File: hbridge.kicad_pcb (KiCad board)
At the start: 2 copper layers, 25.4 x 25.4 mm, 18 parts, among them J1 Conn_01x04_Male, J2 Screw_Terminal_01x03, Q1 2N7000, Q2 2N7000, Q3 2N3904, Q4 2N3906, Q5 2N3904, Q6 2N3906, Q7 STP20NF06, Q8 STP20NF06

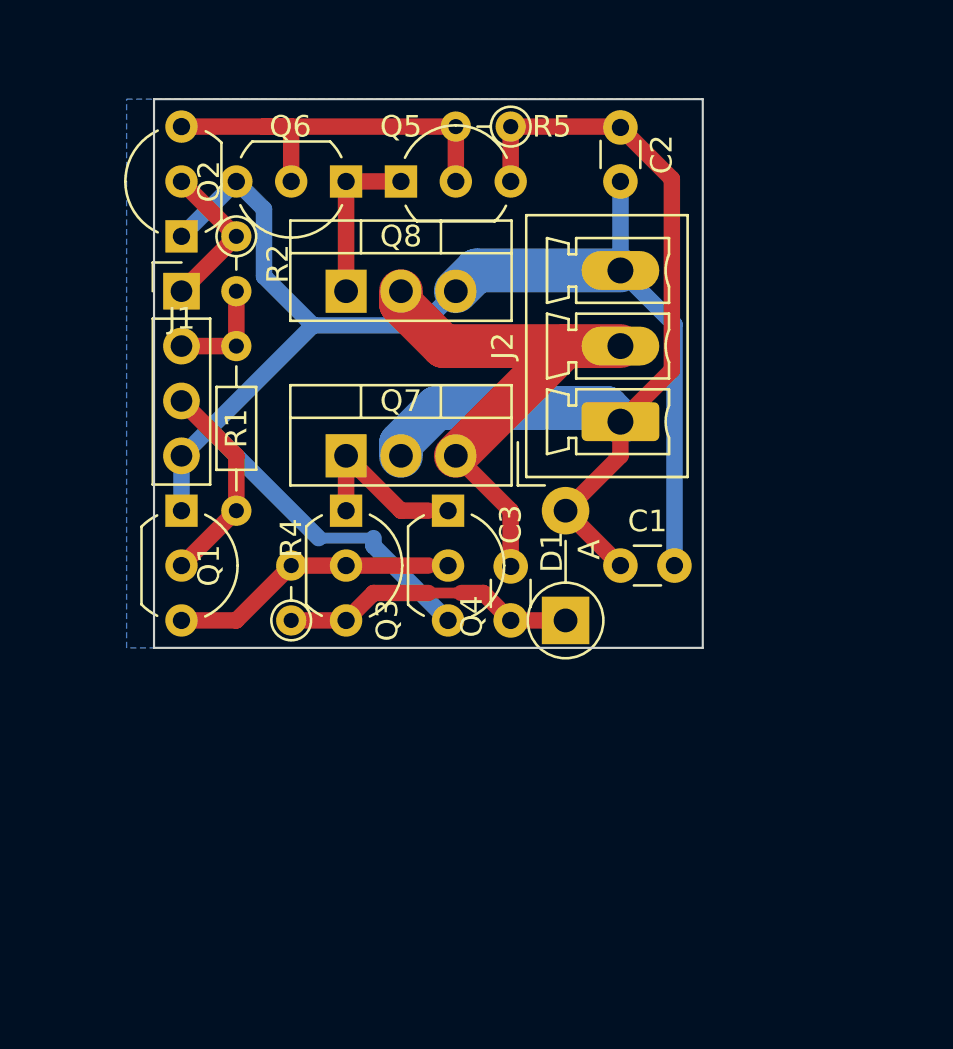
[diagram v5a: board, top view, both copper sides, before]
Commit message: Added second half-bridge to make h-bridge. Not routed yet
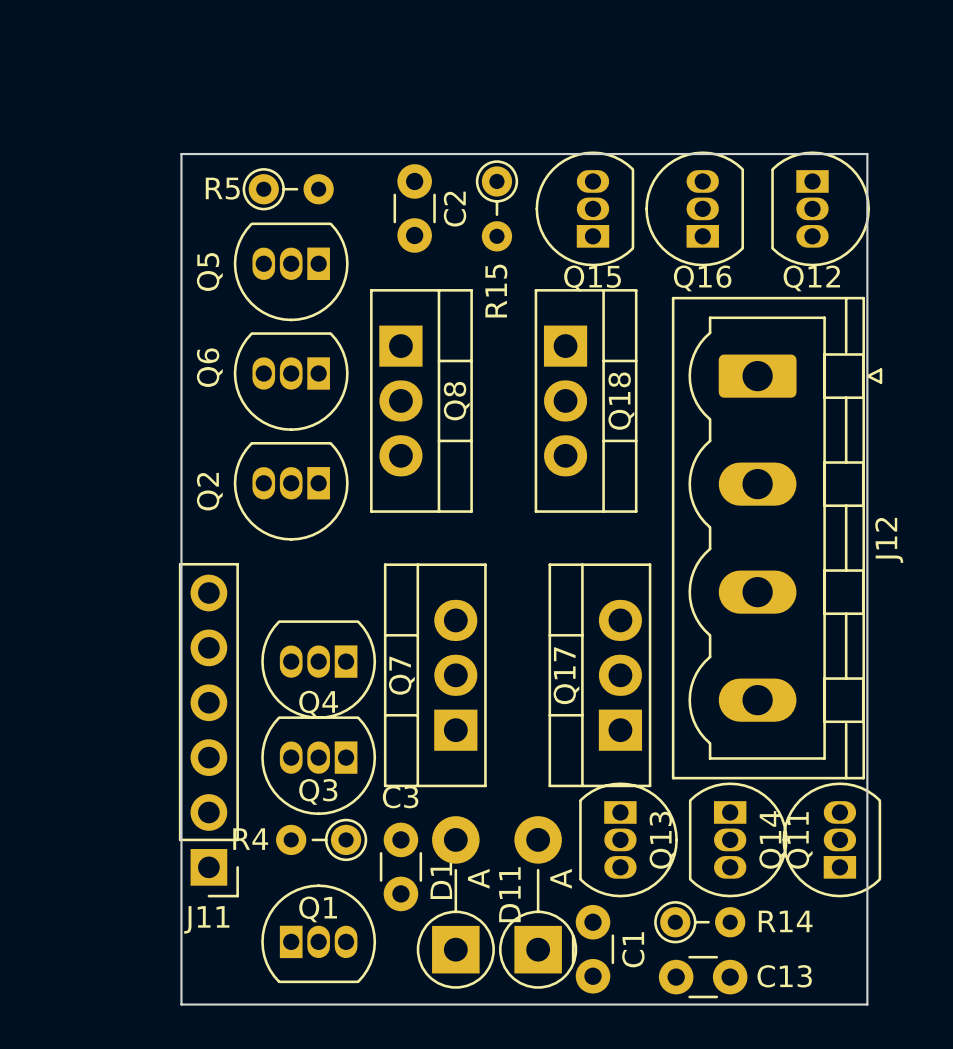
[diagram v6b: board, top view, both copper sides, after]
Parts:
- removed J1: Conn_01x04_Male, Connector_PinHeader_2.54mm:PinHeader_1x04_P2.54mm_Vertical
- removed J2: Screw_Terminal_01x03, Connector_Phoenix_MC:PhoenixContact_MCV_1,5_3-G-3.5_1x03_P3.50mm_Vertical
- removed R1: 10k, Resistor_THT:R_Axial_DIN0204_L3.6mm_D1.6mm_P7.62mm_Horizontal
- removed R2: 10k, Resistor_THT:R_Axial_DIN0204_L3.6mm_D1.6mm_P2.54mm_Vertical
- added C13: 1u, Capacitor_THT:C_Disc_D3.0mm_W1.6mm_P2.50mm, F.Cu at (124.5, 92.7)
- added D11: 1N5819, Diode_THT:D_DO-41_SOD81_P5.08mm_Vertical_AnodeUp, F.Cu at (118.1, 91.4)
- added J11: Conn_01x06_Male, Connector_PinHeader_2.54mm:PinHeader_1x06_P2.54mm_Vertical, F.Cu at (102.9, 87.6)
- added J12: Screw_Terminal_01x04, Connector_Phoenix_MSTB:PhoenixContact_MSTBVA_2,5_4-G_1x04_P5.00mm_Vertical, F.Cu at (128.3, 64.9)
- added Q11: 2N7000, Package_TO_SOT_THT:TO-92_Inline, F.Cu at (132.1, 87.6)
- added Q12: 2N7000, Package_TO_SOT_THT:TO-92_Inline, F.Cu at (130.8, 55.9)
- added Q13: 2N3904, Package_TO_SOT_THT:TO-92_Inline, F.Cu at (121.9, 85.1)
- added Q14: 2N3906, Package_TO_SOT_THT:TO-92_Inline, F.Cu at (127.0, 85.1)
- added Q15: 2N3904, Package_TO_SOT_THT:TO-92_Inline, F.Cu at (120.7, 58.4)
- added Q16: 2N3906, Package_TO_SOT_THT:TO-92_Inline, F.Cu at (125.7, 58.4)
- added Q17: STP20NF06, Package_TO_SOT_THT:TO-220-3_Vertical, F.Cu at (121.9, 81.3)
- added Q18: STP20NF06, Package_TO_SOT_THT:TO-220-3_Vertical, F.Cu at (119.4, 63.5)
- added R14: 10k, Resistor_THT:R_Axial_DIN0204_L3.6mm_D1.6mm_P2.54mm_Vertical, F.Cu at (124.5, 90.2)
- added R15: 10k, Resistor_THT:R_Axial_DIN0204_L3.6mm_D1.6mm_P2.54mm_Vertical, F.Cu at (116.2, 55.9)
- Q1, Q2, Q3, Q4, Q5, Q6: footprint Package_TO_SOT_THT:TO-92_Inline_Wide -> Package_TO_SOT_THT:TO-92_Inline
- moved Q1 20.6 mm to (106.7, 91.1), turned to 0 degrees
- moved C1 16.6 mm to (120.7, 90.2), turned to -90 degrees
- moved D1 16.1 mm to (114.3, 91.4)
- moved Q7 13.7 mm to (114.3, 81.3), turned to 90 degrees
- moved C3 13.6 mm to (111.8, 88.9)
- moved Q2 13.1 mm to (108.0, 69.8), turned to 180 degrees
- moved R5 11.8 mm to (105.4, 56.2), turned to 0 degrees
- moved Q3 11.4 mm to (109.2, 82.5), turned to 180 degrees
- moved R4 10.5 mm to (109.2, 86.4), turned to 180 degrees
- moved C2 9.85 mm to (112.4, 55.9)
- moved Q6 8.98 mm to (108.0, 64.8)
- moved Q4 8.43 mm to (109.2, 78.1), turned to 180 degrees
- moved Q5 5.39 mm to (108.0, 59.7), turned to 180 degrees
- moved Q8 3.59 mm to (111.8, 63.5), turned to -90 degrees
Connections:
- net /Vout renamed /OUT1
- net /boot renamed /boot1
- net /drvH renamed /drvH1
- net /drvL renamed /drvL1
- Q1 pad 2: /PWM -> /H1
- Q2 pad 2: /~PWM~ -> /L1
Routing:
- net GND: track 71.9 -> 0.00 mm
- net +12V: track 43.7 -> 0.00 mm
- net /OUT1: track 24.9 -> 0.00 mm
- net Net-(Q2-Pad3): track 19.1 -> 0.00 mm
- net /boot1: track 13.8 -> 0.00 mm
- net Net-(Q1-Pad3): track 12.5 -> 0.00 mm
- net /PWM: track 9.72 -> 0.00 mm
- net /drvL1: track 7.62 -> 0.00 mm
- net /drvH1: track 7.40 -> 0.00 mm
- net /~PWM~: track 7.18 -> 0.00 mm
- net +5V: track 5.08 -> 0.00 mm
- removed copper zone on B.Cu, net GND
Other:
- board size 25.4 x 25.4 mm -> 31.8 x 39.4 mm

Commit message: More compact layout using smd resistors and capacitors
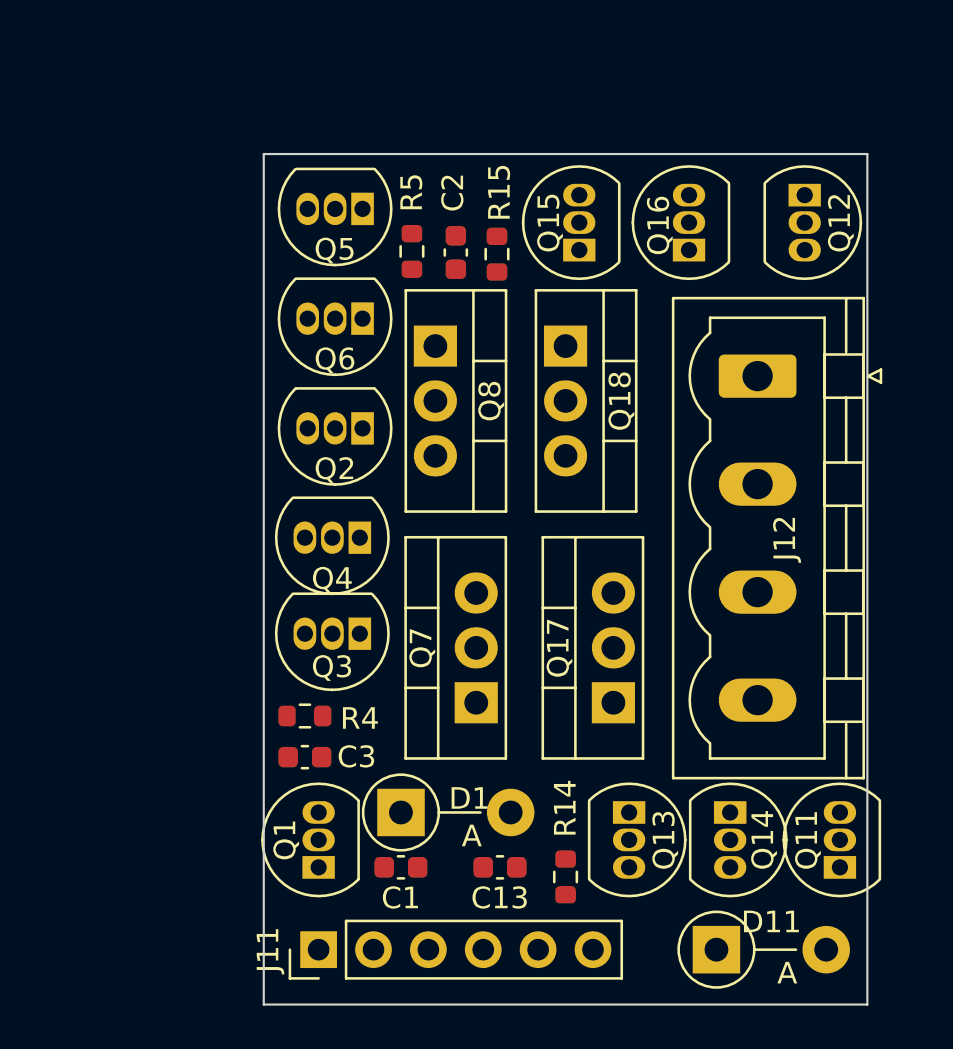
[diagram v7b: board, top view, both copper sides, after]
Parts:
- C1, C13, C2, C3: footprint Capacitor_THT:C_Disc_D3.0mm_W1.6mm_P2.50mm -> Capacitor_SMD:C_0603_1608Metric
- R14, R15, R4, R5: footprint Resistor_THT:R_Axial_DIN0204_L3.6mm_D1.6mm_P2.54mm_Vertical -> Resistor_SMD:R_0603_1608Metric
- moved C13 9.61 mm to (116.3, 87.6), turned to 180 degrees
- moved C1 9.25 mm to (111.8, 87.6), turned to 180 degrees
- moved D11 8.25 mm to (126.4, 91.4), turned to 0 degrees
- moved C3 7.74 mm to (107.3, 82.5), turned to 0 degrees
- moved R5 7.44 mm to (112.3, 59.1), turned to 90 degrees
- moved D1 6.84 mm to (111.8, 85.1), turned to 0 degrees
- moved J11 6.35 mm to (108.0, 91.4), turned to 90 degrees
- moved R4 6.04 mm to (107.3, 80.6), turned to 0 degrees
- moved Q3 5.77 mm to (109.9, 76.8)
- moved Q4 5.77 mm to (109.9, 72.4)
- moved R14 5.50 mm to (119.4, 88.1), turned to 90 degrees
- moved C2 3.80 mm to (114.3, 59.2)
- moved Q1 3.68 mm to (108.0, 87.6), turned to 90 degrees
- moved R15 3.36 mm to (116.2, 59.2)
- moved Q5 3.25 mm to (110.0, 57.1)
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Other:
- board size 31.8 x 39.4 mm -> 27.9 x 39.4 mm

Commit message: Switched diodes to smd
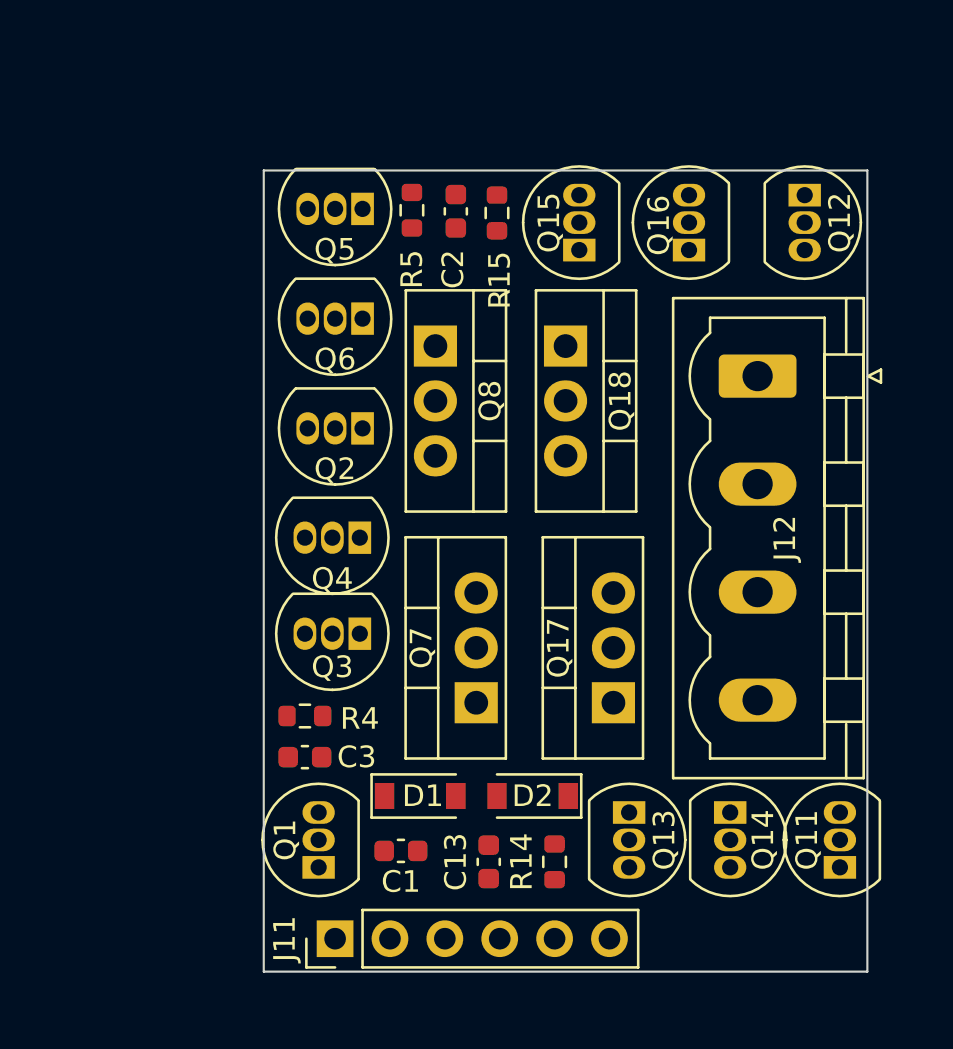
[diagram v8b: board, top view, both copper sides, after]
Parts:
- removed D11: 1N5819, Diode_THT:D_DO-41_SOD81_P5.08mm_Vertical_AnodeUp
- added D2: BAS116GWX, Diode_SMD:D_SOD-123, F.Cu at (117.9, 84.3)
- D1: value 1N5819 -> BAS116GWX; footprint Diode_THT:D_DO-41_SOD81_P5.08mm_Vertical_AnodeUp -> Diode_SMD:D_SOD-123
- moved C2 1.91 mm to (114.3, 57.3)
- moved R15 1.91 mm to (116.2, 57.3)
- moved R5 1.91 mm to (112.3, 57.2)
- moved D1 1.17 mm to (112.7, 84.3)
- moved J11 0.92 mm to (108.7, 90.9)
- moved R14 0.86 mm to (118.9, 87.4)
- moved C1 0.76 mm to (111.8, 86.9)
- moved C13 0.58 mm to (115.8, 87.4), turned to -90 degrees
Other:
- board size 27.9 x 39.4 mm -> 27.9 x 37.1 mm
